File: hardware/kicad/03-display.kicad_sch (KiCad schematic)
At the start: 2 parts, among them J4 FPC-16P-0.5mm

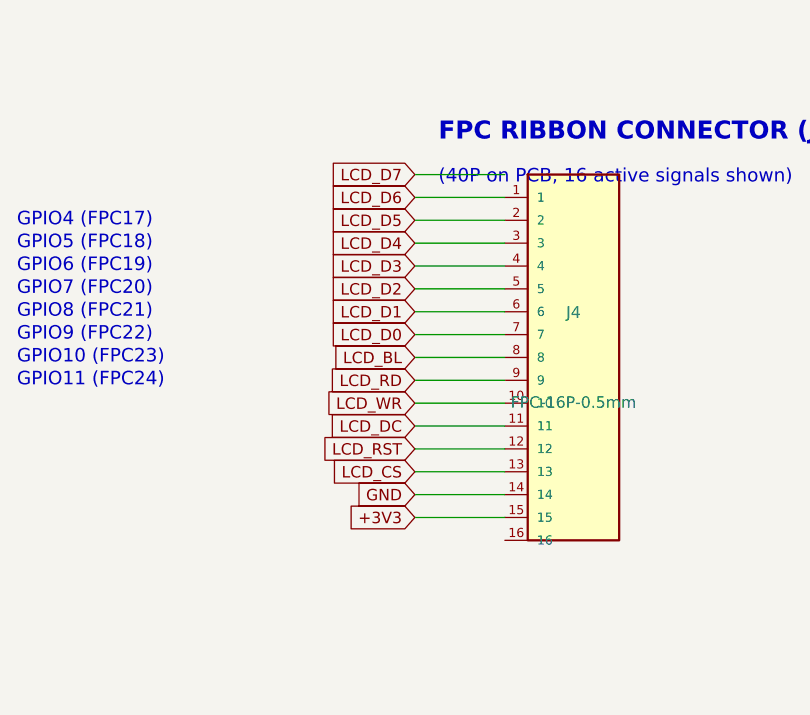
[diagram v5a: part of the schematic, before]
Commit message: sch+tools: fix schematic/PCB pin divergence, recalibrate USB check to Full Speed, make verify-all mean "all"
Failure 1 — verify_netlist_diff T4 (4 mismatches + 2 suppression mechanisms)

Schematic side was wrong in every case; decided from datasheets, not convenience.

* U4 (USBLC6-2SC6, ST doc ID 11265 Rev 5): pins 1/6 are one internal
  I/O node and pins 3/4 the other. The schematic had USB_DM_MCU on
  pin 6 and USB_DP_MCU on pin 4, which shorts R23/R22 out inside the
  package. Both pins of each pair now sit on the connector-side net,
  matching routing.py and hardware/datasheet_specs.py.
* U4 pin 5 is the VBUS clamp reference; the schematic tied it to +5V,
  the IP5306 boost OUTPUT, which is live with no cable attached. Now
  VBUS, as the board already had it.
* U3 (AMS1117): the library symbol used the generic 1=VIN/2=GND/3=VOUT
  numbering. The SOT-223 datasheet land is 1=GND/2=VOUT/3=VIN plus a
  tab (4) that is VOUT. Symbol renumbered, tab pin added; drawing
  unchanged.
* C24/C27/C21 and the twelve button pull-ups R4..R15 had pin 1 and
  pin 2 the opposite way round from their footprints. Symbol
  placement now supports a rotation angle, and these symmetric
  two-terminal parts are placed at 180 deg so the pin numbers agree
  with the pads without altering how the sheet looks.

Real schematic defects found while doing the above:

* Sheets 4 and 5 dropped a GND stub straight through the anchor of the
  label below it: SD_CS was shorted to GND on the SD sheet and the
  PAM8403 audio input was shorted to GND on the audio sheet.
* R22 and R23 were wired with horizontal stubs against a symbol whose
  pins are vertical, so both series termination resistors were
  completely floating in the exported netlist.
* Same class: C22 (the audio DC-block) and the top terminals of
  R20/R21 were attached to nothing.
* The display sheet walked the FPC symbol pins backwards and ran one
  step off the end, so LCD_D7 never reached J4 — the schematic showed
  a 7-bit data bus. I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
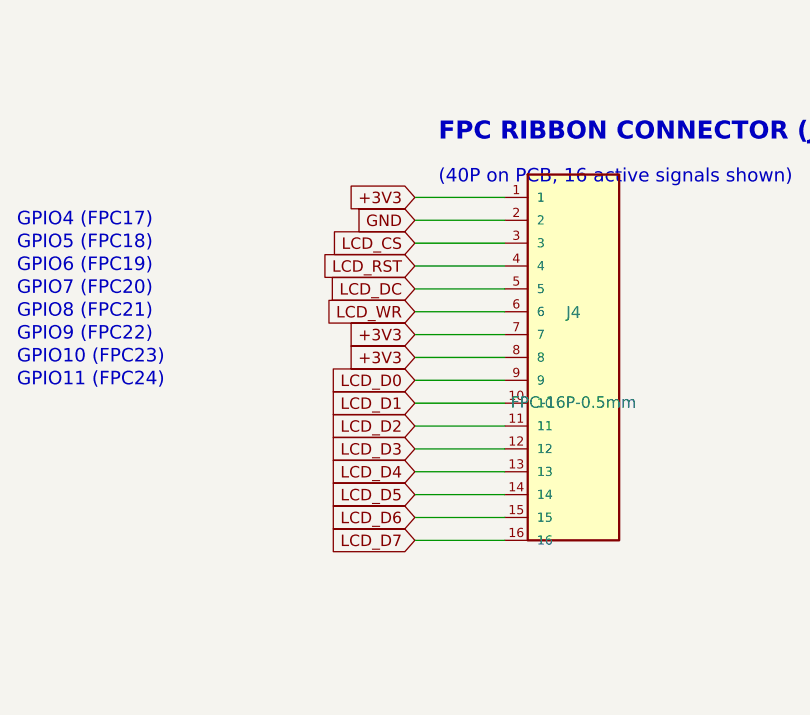
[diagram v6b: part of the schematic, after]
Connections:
- net +3V3: now also J4.1, J4.7, J4.8; no longer J4.15
- net GND: now also J4.2; no longer J4.14
- net LCD_BL: no longer J4.8
- net LCD_CS: now also J4.3; no longer J4.13
- net LCD_D0: now also J4.9; no longer J4.7
- net LCD_D1: now also J4.10; no longer J4.6
- net LCD_D2: now also J4.11; no longer J4.5
- net LCD_D3: now also J4.12; no longer J4.4
- net LCD_D4: now also J4.13; no longer J4.3
- net LCD_D5: now also J4.14; no longer J4.2
- net LCD_D6: now also J4.15; no longer J4.1
- net LCD_D7: now also J4.16
- net LCD_DC: now also J4.5; no longer J4.11
- net LCD_RD: no longer J4.9
- net LCD_RST: now also J4.4; no longer J4.12
- net LCD_WR: now also J4.6; no longer J4.10
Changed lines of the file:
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@@
   (generator "eeschema")
   (generator_version "9.0")
-  (paper "A4")
+  (paper "A3")
   (title_block
     (title "Display - ILI9488 4.0in 8080 Parallel")
@@
   (text "(40P on PCB, 16 active signals shown)" (at 245 100 0) (effects (font (size 1.5 1.5)) (justify left)))
   (symbol (lib_id "FPC_16P") (at 260 120 0) (unit 1) (exclude_from_sim no) (in_bom yes) (on_board yes) (dnp no) (property "Reference" "J4" (at 260 115 0) (effects (font (size 1.27 1.27)))) (property "Value" "FPC-16P-0.5mm" (at 260 125 0) (effects (font (size 1.27 1.27)))) (pin "1") (pin "2") (pin "3") (pin "4") (pin "5") (pin "6") (pin "7") (pin "8") (pin "9") (pin "10") (pin "11") (pin "12") (pin "13") (pin "14") (pin "15") (pin "16"))
-  (global_label "+3V3" (shape input) (at 242.38 137.78 180) (effects (font (size 1.27 1.27))) (property "Intersheetrefs" "" (at 0 0 0) (effects (font (size 1.27 1.27)) hide)))
+  (global_label "+3V3" (shape input) (at 242.38 102.22 180) (effects (font (size 1.27 1.27))) (property "Intersheetrefs" "" (at 0 0 0) (effects (font (size 1.27 1.27)) hide)))
+  (wire (pts (xy 252.38 102.22) (xy 242.38 102.22)) (stroke (width 0) (type default)))
+  (global_label "GND" (shape input) (at 242.38 104.76 180) (effects (font (size 1.27 1.27))) (property "Intersheetrefs" "" (at 0 0 0) (effects (font (size 1.27 1.27)) hide)))
+  (wire (pts (xy 252.38 104.76) (xy 242.38 104.76)) (stroke (width 0) (type default)))
+  (global_label "LCD_CS" (shape input) (at 242.38 107.3 180) (effects (font (size 1.27 1.27))) (property "Intersheetrefs" "" (at 0 0 0) (effects (font (size 1.27 1.27)) hide)))
+  (wire (pts (xy 252.38 107.3) (xy 242.38 107.3)) (stroke (width 0) (type default)))
+  (global_label "LCD_RST" (shape input) (at 242.38 109.84 180) (effects (font (size 1.27 1.27))) (property "Intersheetrefs" "" (at 0 0 0) (effects (font (size 1.27 1.27)) hide)))
+  (wire (pts (xy 252.38 109.84) (xy 242.38 109.84)) (stroke (width 0) (type default)))
+  (global_label "LCD_DC" (shape input) (at 242.38 112.38 180) (effects (font (size 1.27 1.27))) (property "Intersheetrefs" "" (at 0 0 0) (effects (font (size 1.27 1.27)) hide)))
+  (wire (pts (xy 252.38 112.38) (xy 242.38 112.38)) (stroke (width 0) (type default)))
+  (global_label "LCD_WR" (shape input) (at 242.38 114.92 180) (effects (font (size 1.27 1.27))) (property "Intersheetrefs" "" (at 0 0 0) (effects (font (size 1.27 1.27)) hide)))
+  (wire (pts (xy 252.38 114.92) (xy 242.38 114.92)) (stroke (width 0) (type default)))
+  (global_label "+3V3" (shape input) (at 242.38 117.46 180) (effects (font (size 1.27 1.27))) (property "Intersheetrefs" "" (at 0 0 0) (effects (font (size 1.27 1.27)) hide)))
+  (wire (pts (xy 252.38 117.46) (xy 242.38 117.46)) (stroke (width 0) (type default)))
+  (global_label "+3V3" (shape input) (at 242.38 120.0 180) (effects (font (size 1.27 1.27))) (property "Intersheetrefs" "" (at 0 0 0) (effects (font (size 1.27 1.27)) hide)))
+  (wire (pts (xy 252.38 120.0) (xy 242.38 120.0)) (stroke (width 0) (type default)))
+  (global_label "LCD_D0" (shape input) (at 242.38 122.53999999999999 180) (effects (font (size 1.27 1.27))) (property "Intersheetrefs" "" (at 0 0 0) (effects (font (size 1.27 1.27)) hide)))
+  (wire (pts (xy 252.38 122.53999999999999) (xy 242.38 122.53999999999999)) (stroke (width 0) (type default)))
+  (global_label "LCD_D1" (shape input) (at 242.38 125.08 180) (effects (font (size 1.27 1.27))) (property "Intersheetrefs" "" (at 0 0 0) (effects (font (size 1.27 1.27)) hide)))
+  (wire (pts (xy 252.38 125.08) (xy 242.38 125.08)) (stroke (width 0) (type default)))
+  (global_label "LCD_D2" (shape input) (at 242.38 127.62 180) (effects (font (size 1.27 1.27))) (property "Intersheetrefs" "" (at 0 0 0) (effects (font (size 1.27 1.27)) hide)))
+  (wire (pts (xy 252.38 127.62) (xy 242.38 127.62)) (stroke (width 0) (type default)))
+  (global_label "LCD_D3" (shape input) (at 242.38 130.16 180) (effects (font (size 1.27 1.27))) (property "Intersheetrefs" "" (at 0 0 0) (effects (font (size 1.27 1.27)) hide)))
+  (wire (pts (xy 252.38 130.16) (xy 242.38 130.16)) (stroke (width 0) (type default)))
+  (global_label "LCD_D4" (shape input) (at 242.38 132.7 180) (effects (font (size 1.27 1.27))) (property "Intersheetrefs" "" (at 0 0 0) (effects (font (size 1.27 1.27)) hide)))
+  (wire (pts (xy 252.38 132.7) (xy 242.38 132.7)) (stroke (width 0) (type default)))
+  (global_label "LCD_D5" (shape input) (at 242.38 135.24 180) (effects (font (size 1.27 1.27))) (property "Intersheetrefs" "" (at 0 0 0) (effects (font (size 1.27 1.27)) hide)))
+  (wire (pts (xy 252.38 135.24) (xy 242.38 135.24)) (stroke (width 0) (type default)))
+  (global_label "LCD_D6" (shape input) (at 242.38 137.78 180) (effects (font (size 1.27 1.27))) (property "Intersheetrefs" "" (at 0 0 0) (effects (font (size 1.27 1.27)) hide)))
   (wire (pts (xy 252.38 137.78) (xy 242.38 137.78)) (stroke (width 0) (type default)))
-  (global_label "GND" (shape input) (at 242.38 135.24 180) (effects (font (size 1.27 1.27))) (property "Intersheetrefs" "" (at 0 0 0) (effects (font (size 1.27 1.27)) hide)))
-  (wire (pts (xy 252.38 135.24) (xy 242.38 135.24)) (stroke (width 0) (type default)))
-  (global_label "LCD_CS" (shape input) (at 242.38 132.7 180) (effects (font (size 1.27 1.27))) (property "Intersheetrefs" "" (at 0 0 0) (effects (font (size 1.27 1.27)) hide)))
-  (wire (pts (xy 252.38 132.7) (xy 242.38 132.7)) (stroke (width 0) (type default)))
-  (global_label "LCD_RST" (shape input) (at 242.38 130.16 180) (effects (font (size 1.27 1.27))) (property "Intersheetrefs" "" (at 0 0 0) (effects (font (size 1.27 1.27)) hide)))
-  (wire (pts (xy 252.38 130.16) (xy 242.38 130.16)) (stroke (width 0) (type default)))
-  (global_label "LCD_DC" (shape input) (at 242.38 127.62 180) (effects (font (size 1.27 1.27))) (property "Intersheetrefs" "" (at 0 0 0) (effects (font (size 1.27 1.27)) hide)))
-  (wire (pts (xy 252.38 127.62) (xy 242.38 127.62)) (stroke (width 0) (type default)))
-  (global_label "LCD_WR" (shape input) (at 242.38 125.08 180) (effects (font (size 1.27 1.27))) (property "Intersheetrefs" "" (at 0 0 0) (effects (font (size 1.27 1.27)) hide)))
-  (wire (pts (xy 252.38 125.08) (xy 242.38 125.08)) (stroke (width 0) (type default)))
-  (global_label "LCD_RD" (shape input) (at 242.38 122.54 180) (effects (font (size 1.27 1.27))) (property "Intersheetrefs" "" (at 0 0 0) (effects (font (size 1.27 1.27)) hide)))
-  (wire (pts (xy 252.38 122.54) (xy 242.38 122.54)) (stroke (width 0) (type default)))
-  (global_label "LCD_BL" (shape input) (at 242.38 120.0 180) (effects (font (size 1.27 1.27))) (property "Intersheetrefs" "" (at 0 0 0) (effects (font (size 1.27 1.27)) hide)))
-  (wire (pts (xy 252.38 120.0) (xy 242.38 120.0)) (stroke (width 0) (type default)))
-  (global_label "LCD_D0" (shape input) (at 242.38 117.46000000000001 180) (effects (font (size 1.27 1.27))) (property "Intersheetrefs" "" (at 0 0 0) (effects (font (size 1.27 1.27)) hide)))
-  (wire (pts (xy 252.38 117.46000000000001) (xy 242.38 117.46000000000001)) (stroke (width 0) (type default)))
-  (global_label "LCD_D1" (shape input) (at 242.38 114.92 180) (effects (font (size 1.27 1.27))) (property "Intersheetrefs" "" (at 0 0 0) (effects (font (size 1.27 1.27)) hide)))
-  (wire (pts (xy 252.38 114.92) (xy 242.38 114.92)) (stroke (width 0) (type default)))
-  (global_label "LCD_D2" (shape input) (at 242.38 112.38 180) (effects (font (size 1.27 1.27))) (property "Intersheetrefs" "" (at 0 0 0) (effects (font (size 1.27 1.27)) hide)))
-  (wire (pts (xy 252.38 112.38) (xy 242.38 112.38)) (stroke (width 0) (type default)))
-  (global_label "LCD_D3" (shape input) (at 242.38 109.84 180) (effects (font (size 1.27 1.27))) (property "Intersheetrefs" "" (at 0 0 0) (effects (font (size 1.27 1.27)) hide)))
-  (wire (pts (xy 252.38 109.84) (xy 242.38 109.84)) (stroke (width 0) (type default)))
-  (global_label "LCD_D4" (shape input) (at 242.38 107.3 180) (effects (font (size 1.27 1.27))) (property "Intersheetrefs" "" (at 0 0 0) (effects (font (size 1.27 1.27)) hide)))
-  (wire (pts (xy 252.38 107.3) (xy 242.38 107.3)) (stroke (width 0) (type default)))
-  (global_label "LCD_D5" (shape input) (at 242.38 104.75999999999999 180) (effects (font (size 1.27 1.27))) (property "Intersheetrefs" "" (at 0 0 0) (effects (font (size 1.27 1.27)) hide)))
-  (wire (pts (xy 252.38 104.75999999999999) (xy 242.38 104.75999999999999)) (stroke (width 0) (type default)))
-  (global_label "LCD_D6" (shape input) (at 242.38 102.22 180) (effects (font (size 1.27 1.27))) (property "Intersheetrefs" "" (at 0 0 0) (effects (font (size 1.27 1.27)) hide)))
-  (wire (pts (xy 252.38 102.22) (xy 242.38 102.22)) (stroke (width 0) (type default)))
-  (global_label "LCD_D7" (shape input) (at 242.38 99.68 180) (effects (font (size 1.27 1.27))) (property "Intersheetrefs" "" (at 0 0 0) (effects (font (size 1.27 1.27)) hide)))
-  (wire (pts (xy 252.38 99.68) (xy 242.38 99.68)) (stroke (width 0) (type default)))
+  (global_label "LCD_D7" (shape input) (at 242.38 140.32 180) (effects (font (size 1.27 1.27))) (property "Intersheetrefs" "" (at 0 0 0) (effects (font (size 1.27 1.27)) hide)))
+  (wire (pts (xy 252.38 140.32) (xy 242.38 140.32)) (stroke (width 0) (type default)))
   (text "ILI9488 Panel FPC-40P Pin Mapping (source: components.md):" (at 30 180 0) (effects (font (size 2.54 2.54) bold) (justify left)))
   (text "Panel 6,7=VDDI/VDDA(+3V3)  9=CS  10=DC  11=WR  12=RD  15=RESET" (at 30 188 0) (effects (font (size 2.54 2.54)) (justify left)))
